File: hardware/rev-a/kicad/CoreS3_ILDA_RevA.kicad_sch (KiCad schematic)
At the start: 0 parts

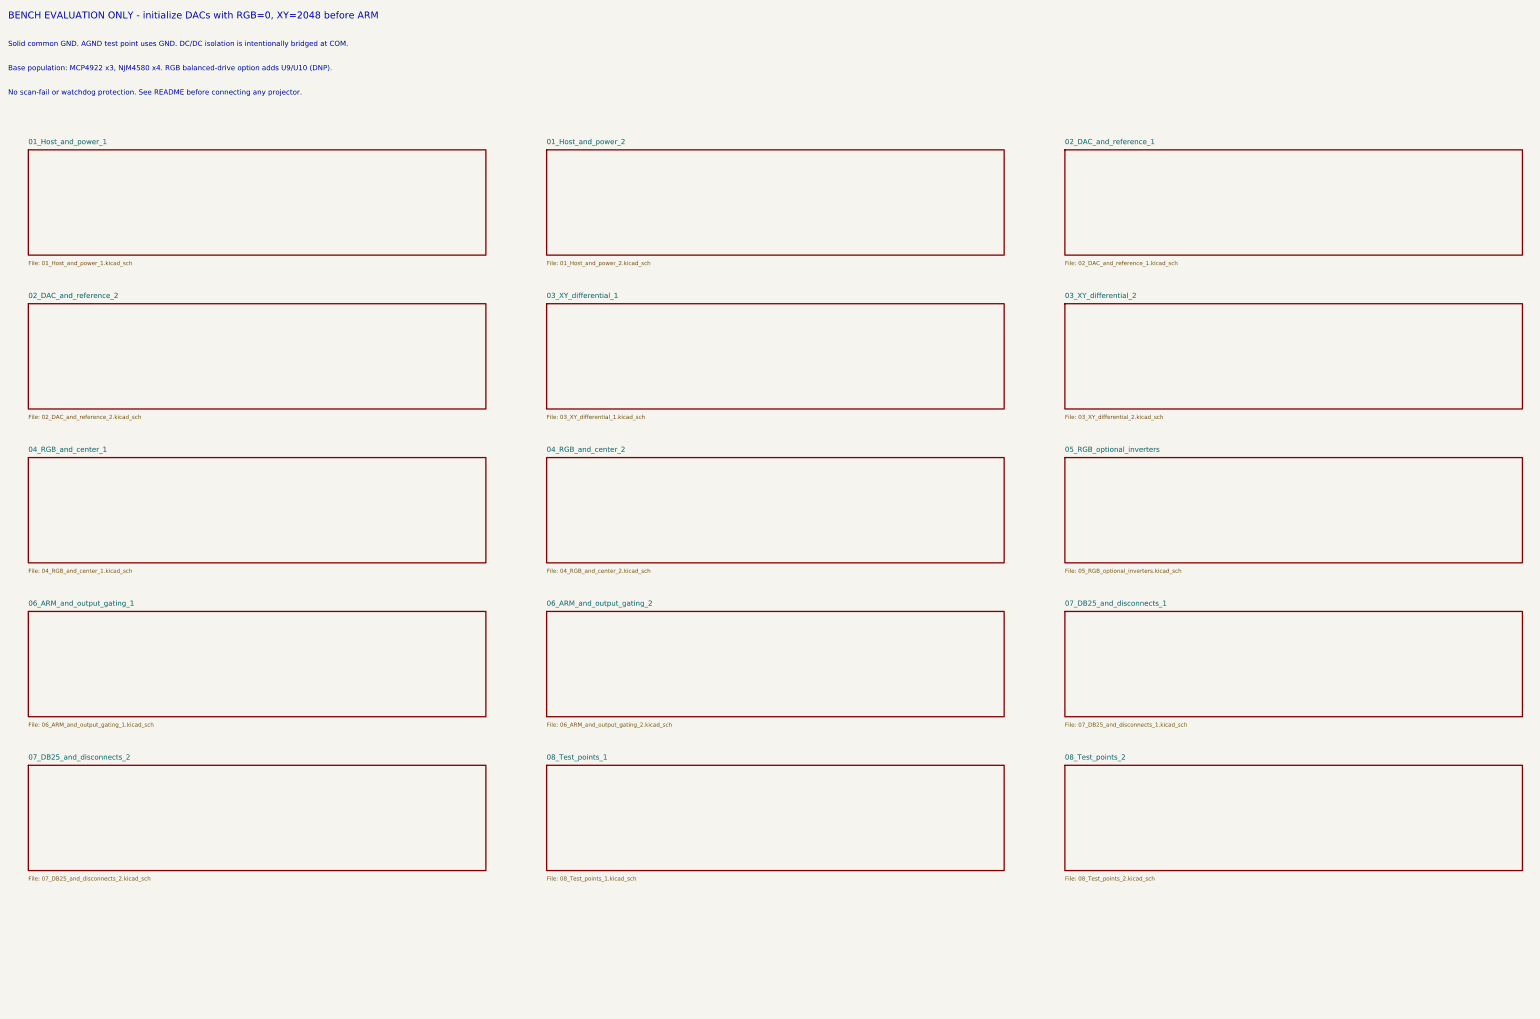
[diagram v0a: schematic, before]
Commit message: Redraw Rev.A schematics with functional blocks and explicit wiring
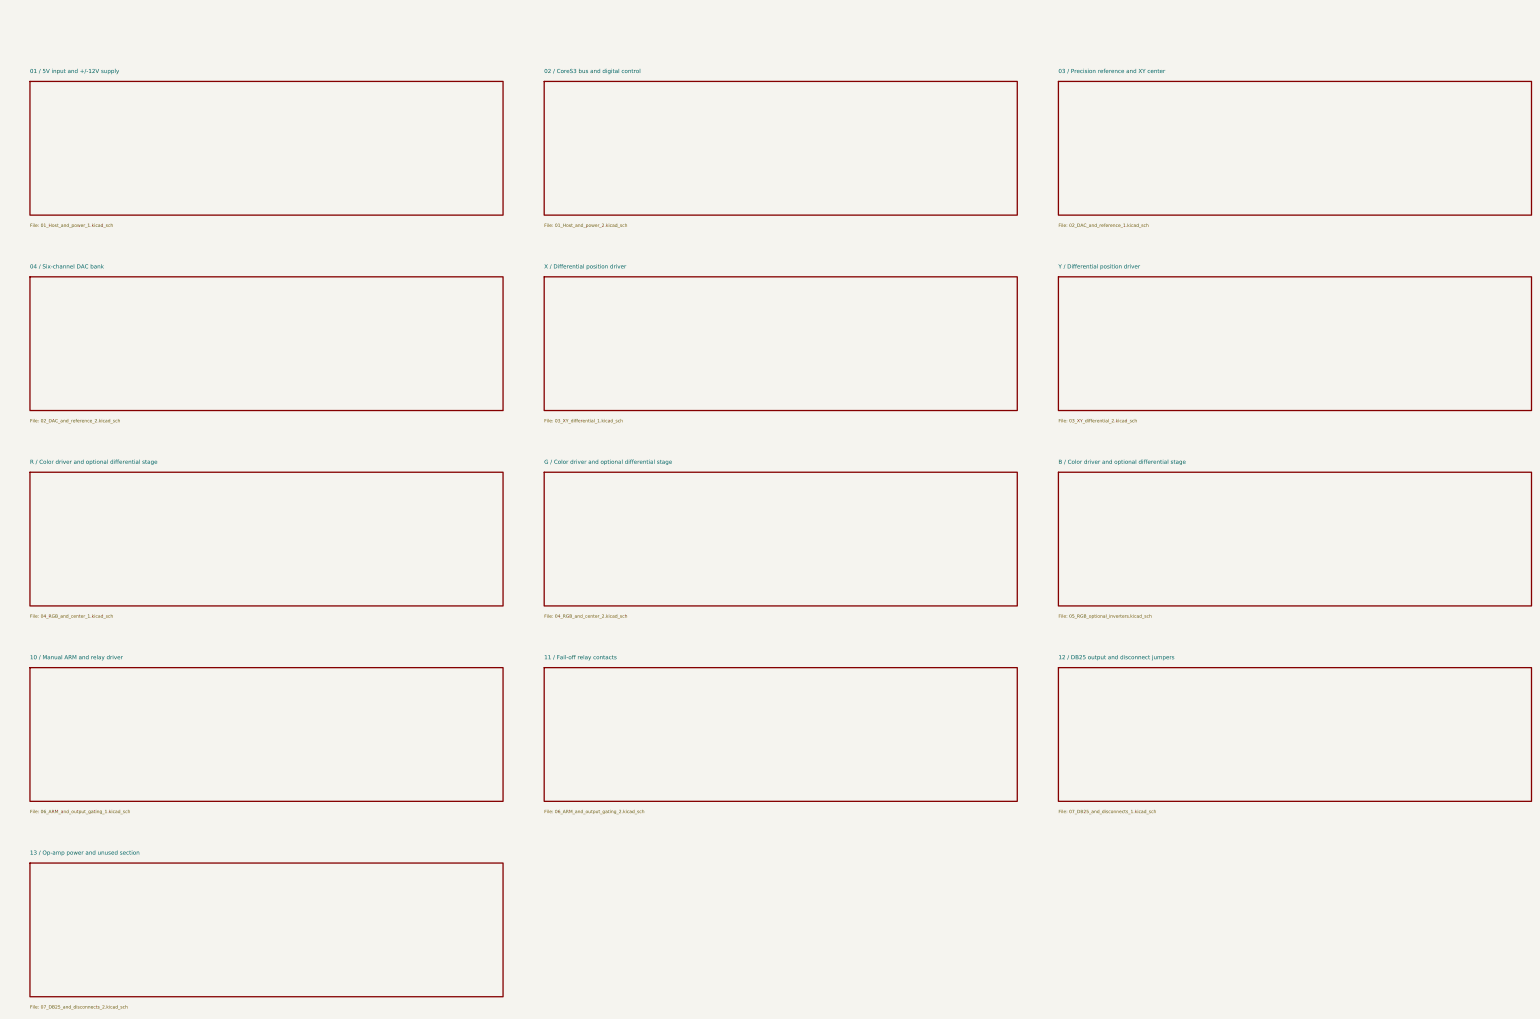
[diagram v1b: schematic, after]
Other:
- removed sheet 01_Host_and_power_1
- removed sheet 01_Host_and_power_2
- removed sheet 02_DAC_and_reference_1
- removed sheet 02_DAC_and_reference_2
- removed sheet 03_XY_differential_1
- removed sheet 03_XY_differential_2
- removed sheet 04_RGB_and_center_1
- removed sheet 04_RGB_and_center_2
- removed sheet 05_RGB_optional_inverters
- removed sheet 06_ARM_and_output_gating_1
- removed sheet 06_ARM_and_output_gating_2
- removed sheet 07_DB25_and_disconnects_1
- removed sheet 07_DB25_and_disconnects_2
- removed sheet 08_Test_points_1
- removed sheet 08_Test_points_2
- added sheet 01 / 5V input and +/-12V supply (01_Host_and_power_1.kicad_sch)
- added sheet 02 / CoreS3 bus and digital control (01_Host_and_power_2.kicad_sch)
- added sheet 03 / Precision reference and XY center (02_DAC_and_reference_1.kicad_sch)
- added sheet 04 / Six-channel DAC bank (02_DAC_and_reference_2.kicad_sch)
- added sheet 10 / Manual ARM and relay driver (06_ARM_and_output_gating_1.kicad_sch)
- added sheet 11 / Fail-off relay contacts (06_ARM_and_output_gating_2.kicad_sch)
- added sheet 12 / DB25 output and disconnect jumpers (07_DB25_and_disconnects_1.kicad_sch)
- added sheet 13 / Op-amp power and unused section (07_DB25_and_disconnects_2.kicad_sch)
- added sheet B / Color driver and optional differential stage (05_RGB_optional_inverters.kicad_sch)
- added sheet G / Color driver and optional differential stage (04_RGB_and_center_2.kicad_sch)
- added sheet R / Color driver and optional differential stage (04_RGB_and_center_1.kicad_sch)
- added sheet X / Differential position driver (03_XY_differential_1.kicad_sch)
- added sheet Y / Differential position driver (03_XY_differential_2.kicad_sch)
- note removed: "BENCH EVALUATION ONLY - initialize DACs with RGB=0, XY=2048 before ARM"
- note removed: "Base population: MCP4922 x3, NJM4580 x4. RGB balanced-drive option adds U9/U10 (DNP)."
- note removed: "No scan-fail or watchdog protection. See README before connecting any projector."
- note removed: "Solid common GND. AGND test point uses GND. DC/DC isolation is intentionally bridged at COM."
- company: CoreS3 ILDA evaluation -> (none)
- title: CoreS3 ILDA Rev.A - design index -> CoreS3 ILDA Rev.A - functional schematics
